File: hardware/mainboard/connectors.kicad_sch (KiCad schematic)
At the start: 25 parts, among them J1 Kenwood-2.5, J10 UART, J11 Radio_Opt, J12 Speaker, J13 KH-RJ45-58-8P8C, J2 USB_C, J301 +12V, J301 2.54mm Header 7p, J412 Hirose FH12-26S-0.5SH(55), J413 Molex 532610271, J5 Kenwood-3.5, J7 Radio, J9 STLink, U401 USBLC6-2SC6

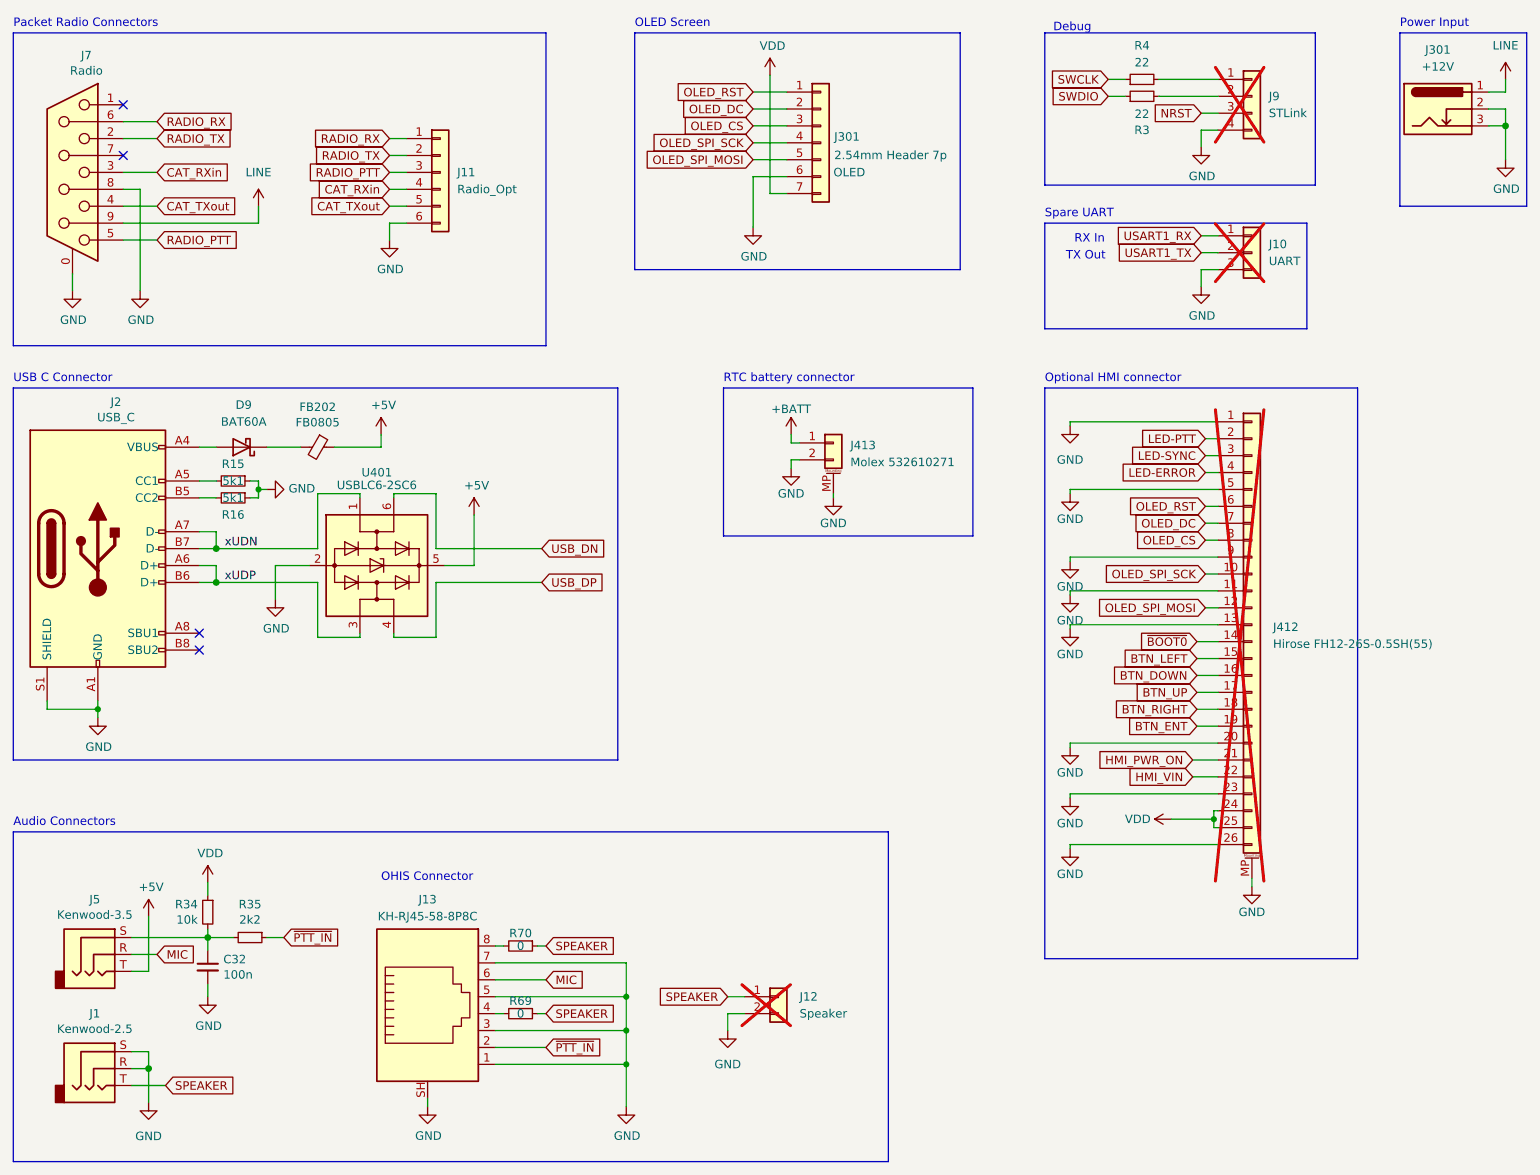
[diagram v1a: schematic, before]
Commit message: Updated mainboard
Replaced OHIS speaker resistors with larger 100 ohms resistors
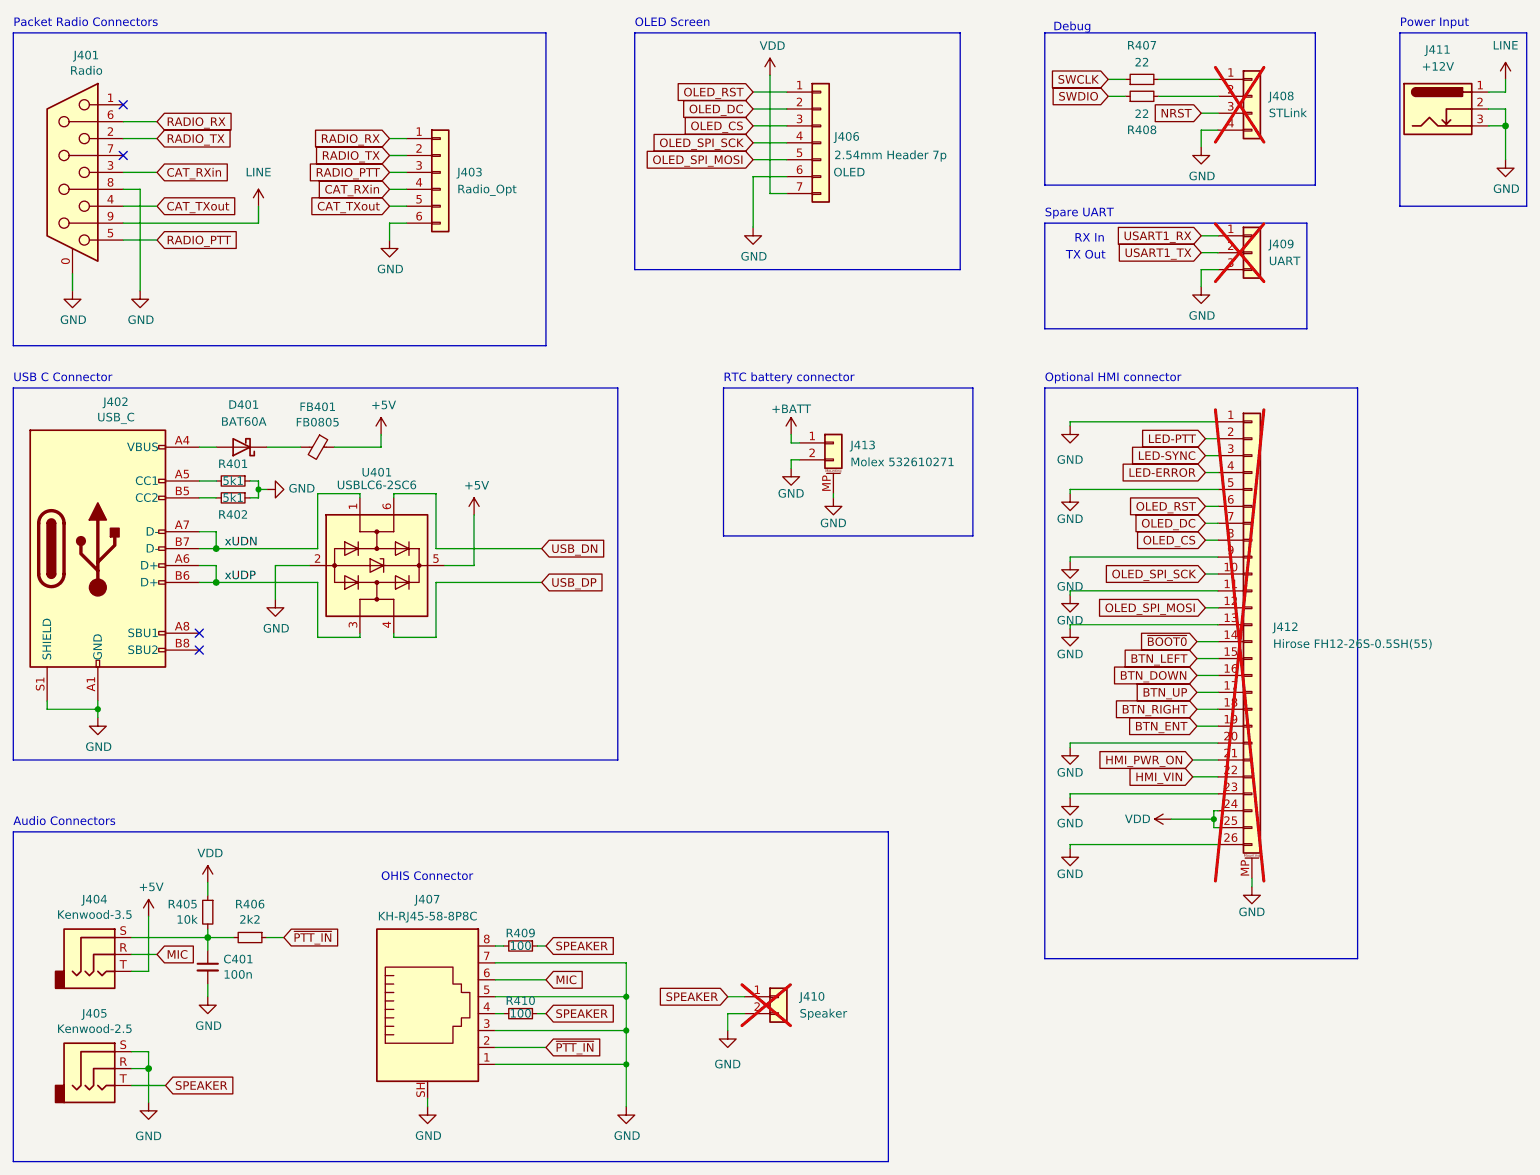
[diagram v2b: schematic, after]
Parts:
- R409: renamed from R70; value 0 -> 100; footprint Resistor_SMD:R_0603_1608Metric -> Resistor_SMD:R_1210_3225Metric
- R410: renamed from R69; value 0 -> 100; footprint Resistor_SMD:R_0603_1608Metric -> Resistor_SMD:R_1210_3225Metric
- renumbered C32 to C401, D9 to D401, FB202 to FB401, J7 to J401, J2 to J402, J11 to J403, J5 to J404, J1 to J405, J301 to J406, J13 to J407, J9 to J408, J10 to J409, J12 to J410, J301 to J411, R15 to R401, R16 to R402, R34 to R405, R35 to R406, R4 to R407, R3 to R408
